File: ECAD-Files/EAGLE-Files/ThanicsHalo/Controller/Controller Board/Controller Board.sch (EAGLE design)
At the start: 179 parts, among them J10 EDGE_CONNECTOR_20POS, J2 USB_A_RECEPT, J3 105450-0101, J5 EDGE_CONNECTOR_20POS, J6 MICROSD, J7 105450-0101, J8 2_PIN_CONNECTOR, J9 B2B-PH-SM4-TB(LF)(SN), Q2 2N7002P_MOSFET, T1 ALT4532M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

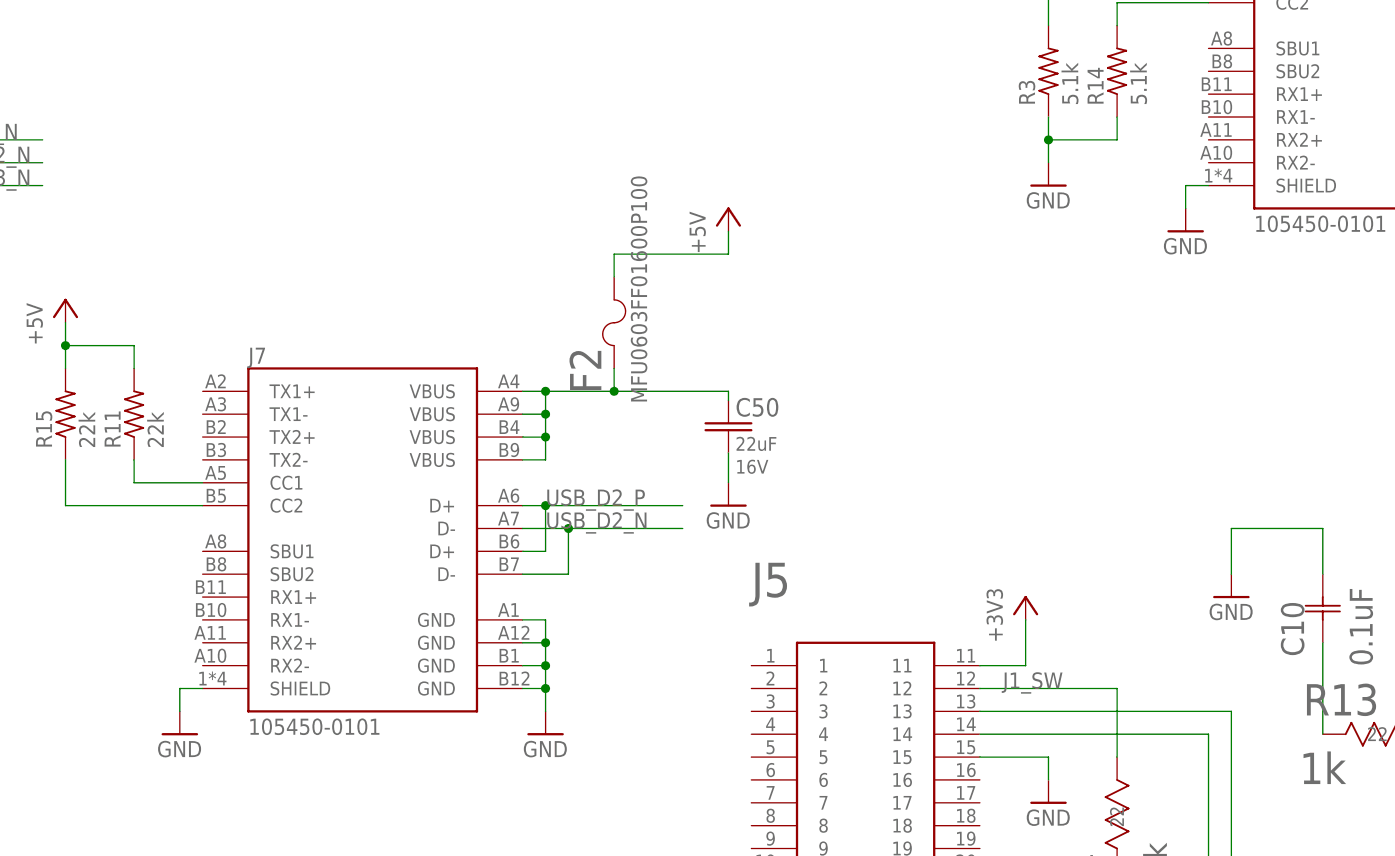
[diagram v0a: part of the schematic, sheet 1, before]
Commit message: Fixed USB C connector sheild pin short problem
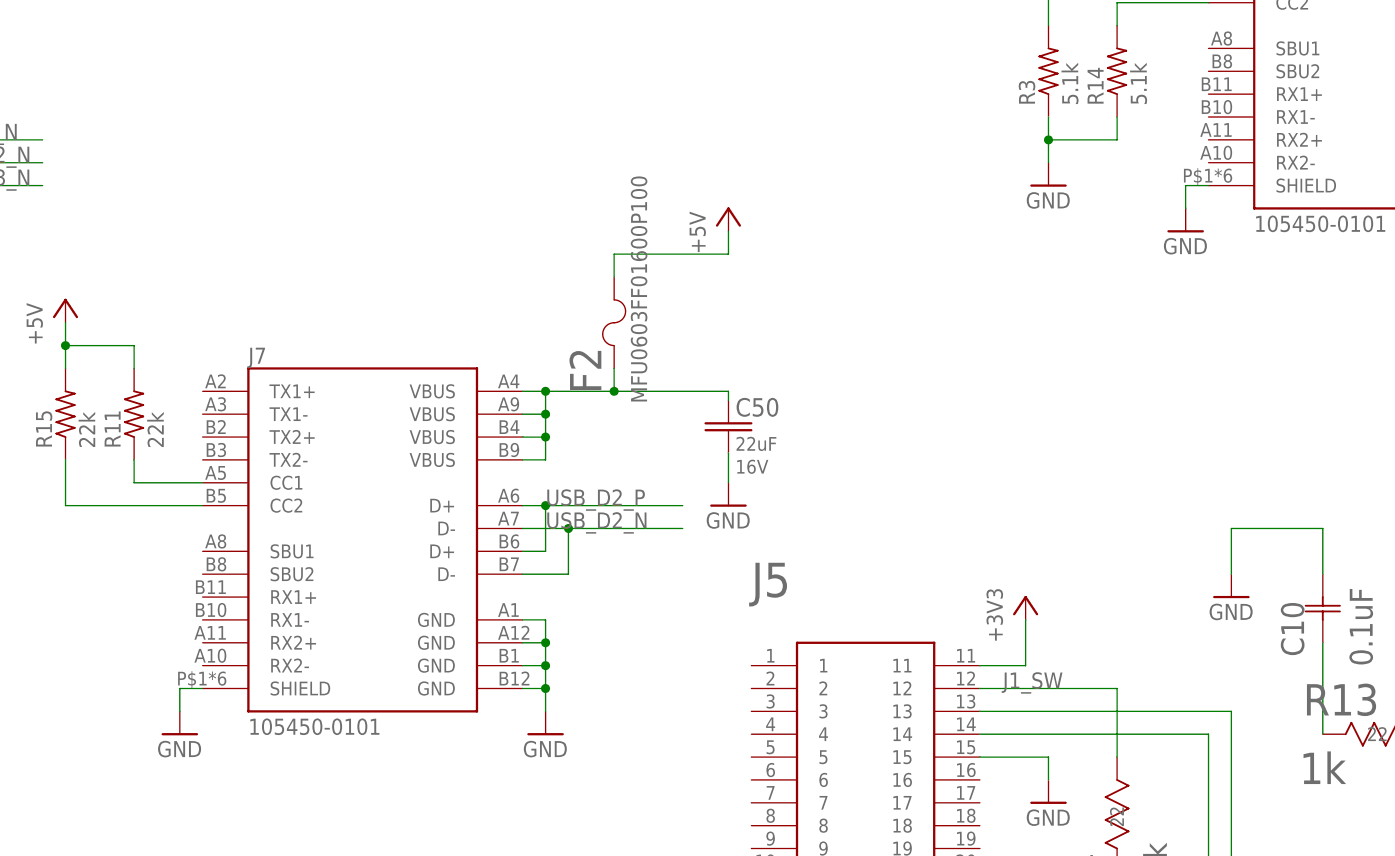
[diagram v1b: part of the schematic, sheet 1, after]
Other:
- moved on the sheet: J3, J7
